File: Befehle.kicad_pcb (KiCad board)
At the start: 2 copper layers, 100 x 160 mm, 36 parts, among them P1 CONN_02X10, P2 CONN_02X10, U1 74LS14, U2 74540, U3 7400, U4 74HCT02, U5 74LS541, U6 74LS373, U7 74LS139, U8 74LS540

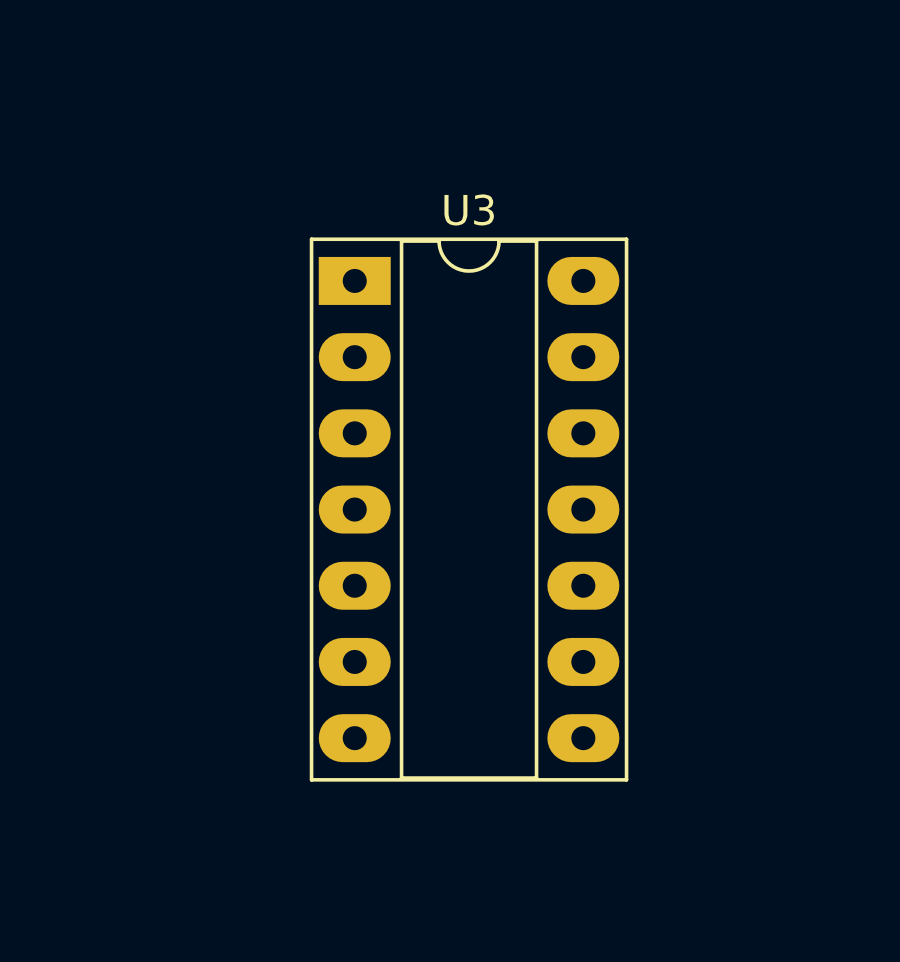
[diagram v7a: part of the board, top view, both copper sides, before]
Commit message: Beschriftungen formatiert
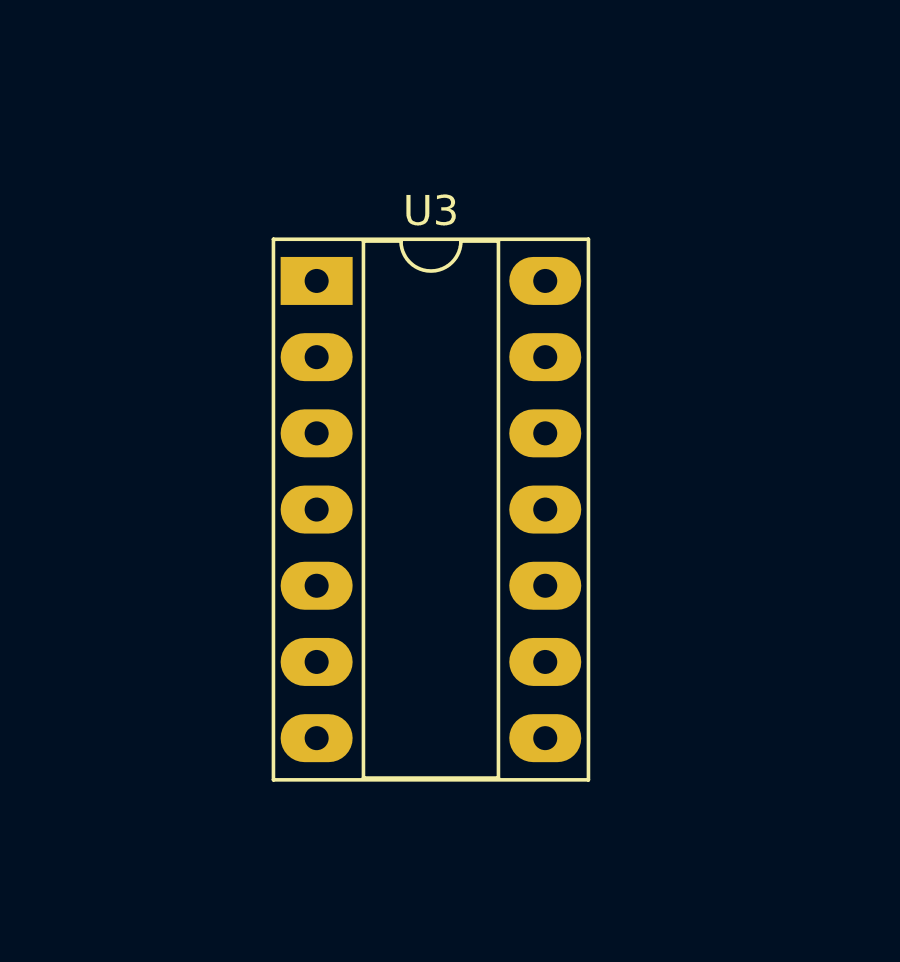
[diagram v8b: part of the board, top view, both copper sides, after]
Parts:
- moved U3 1.27 mm to (33.0, 144.8)
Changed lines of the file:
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@@
-(kicad_pcb (version 4) (host pcbnew 4.0.4+e1-6308~48~ubuntu16.04.1-stable)
+(kicad_pcb (version 4) (host pcbnew 4.0.7)
   (general
     (links 82)
     (no_connects 82)
-    (area 0 0 0 0)
+    (area 17.932 17.409819 119.83 180.288)
     (thickness 1.6)
     (drawings 0)
@@
     (pad_to_mask_clearance 0.2)
     (aux_axis_origin 0 0)
-    (visible_elements FFFFFF7F)
+    (visible_elements 7FFFFFFF)
     (pcbplotparams
       (layerselection 0x00030_80000001)
@@
   )
   (module Housings_DIP:DIP-14_W7.62mm_Socket_LongPads (layer F.Cu)
-    (at 34.29 144.78)
+    (at 33.02 144.78)
     (descr "14-lead though-hole mounted DIP package, row spacing 7.62 mm (300 mils), Socket, LongPads")
     (tags "THT DIP DIL PDIP 2.54mm 7.62mm 300mil Socket LongPads")
